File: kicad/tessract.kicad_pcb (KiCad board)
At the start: 2 copper layers, 35 x 50 mm, 23 parts, among them Q1 DMP1045U, U1 MICRO-B_USB, U2 MCP73832T, U3 MCP1755, U4 ATMEL_ATTINY85_20SU, U5 OSRAM_LRTB_GFTG, U6 HM-10

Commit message: wider track and silkscreen logo
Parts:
- added solderbyte_logo: G***, solderbyte:solderbyte_logo_25mm, F.Cu at (132.8, 74.8)
- added solderbyte_logo: G***, solderbyte:SOLDERBYTE_LOGO_20MM, B.Cu at (132.2, 90.0)

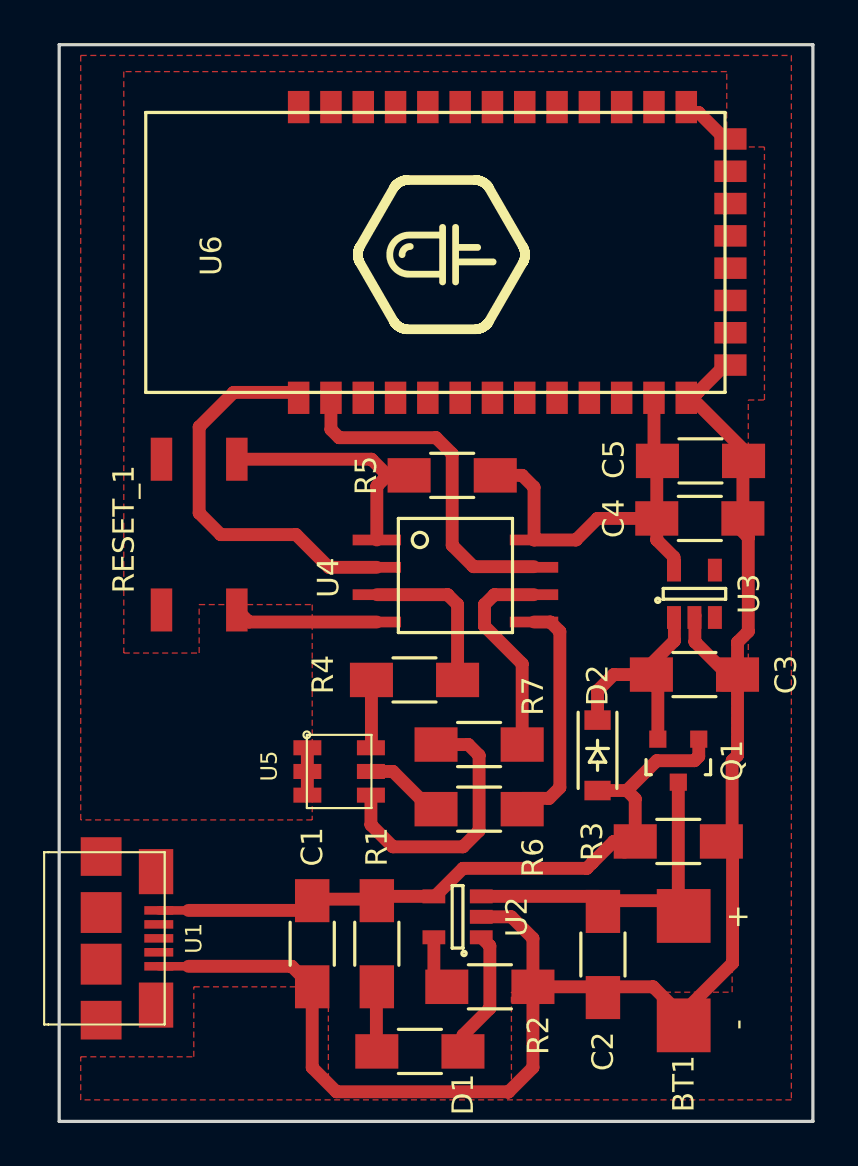
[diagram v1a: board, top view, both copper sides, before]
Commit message: removed library
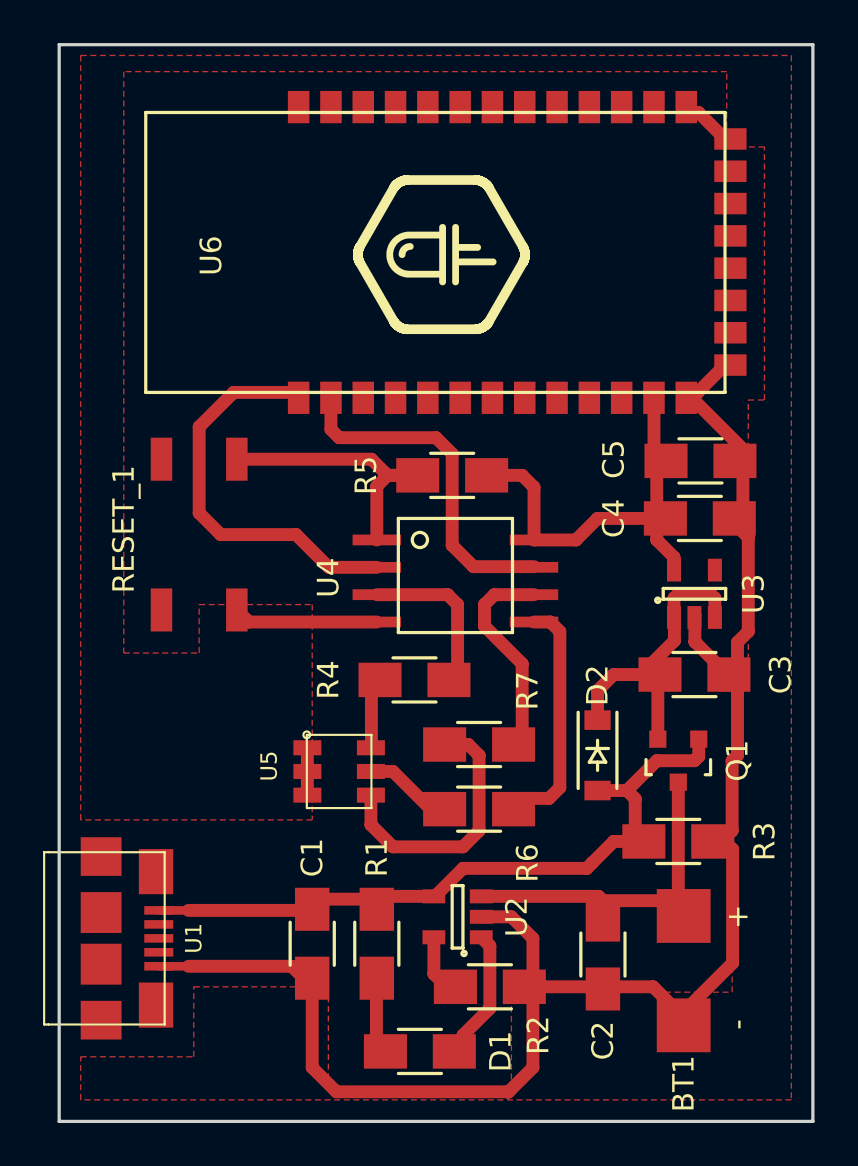
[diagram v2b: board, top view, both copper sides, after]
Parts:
- U1: value MICRO-B_USB -> MICRO_B_USB
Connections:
- U3 pad 3: Net-(U3-Pad3) -> Net-(C3-Pad1)
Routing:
- net Net-(C3-Pad1): track 11.3 -> 15.2 mm
- net Net-(C1-Pad1): track 34.2 -> 33.5 mm
